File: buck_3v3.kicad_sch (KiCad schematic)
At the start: 20 parts, among them U6 TPS564257DRLR

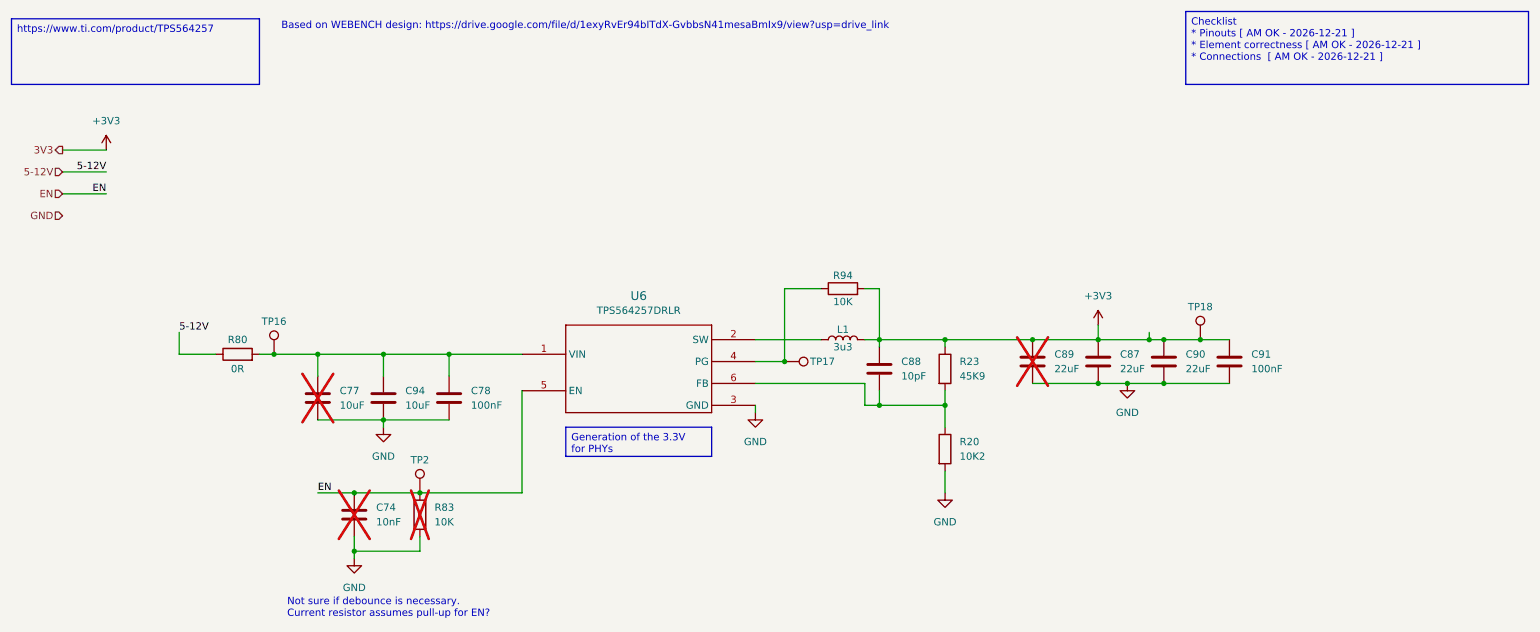
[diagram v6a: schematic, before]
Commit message: fixing issue related to symbol changes, and updating components
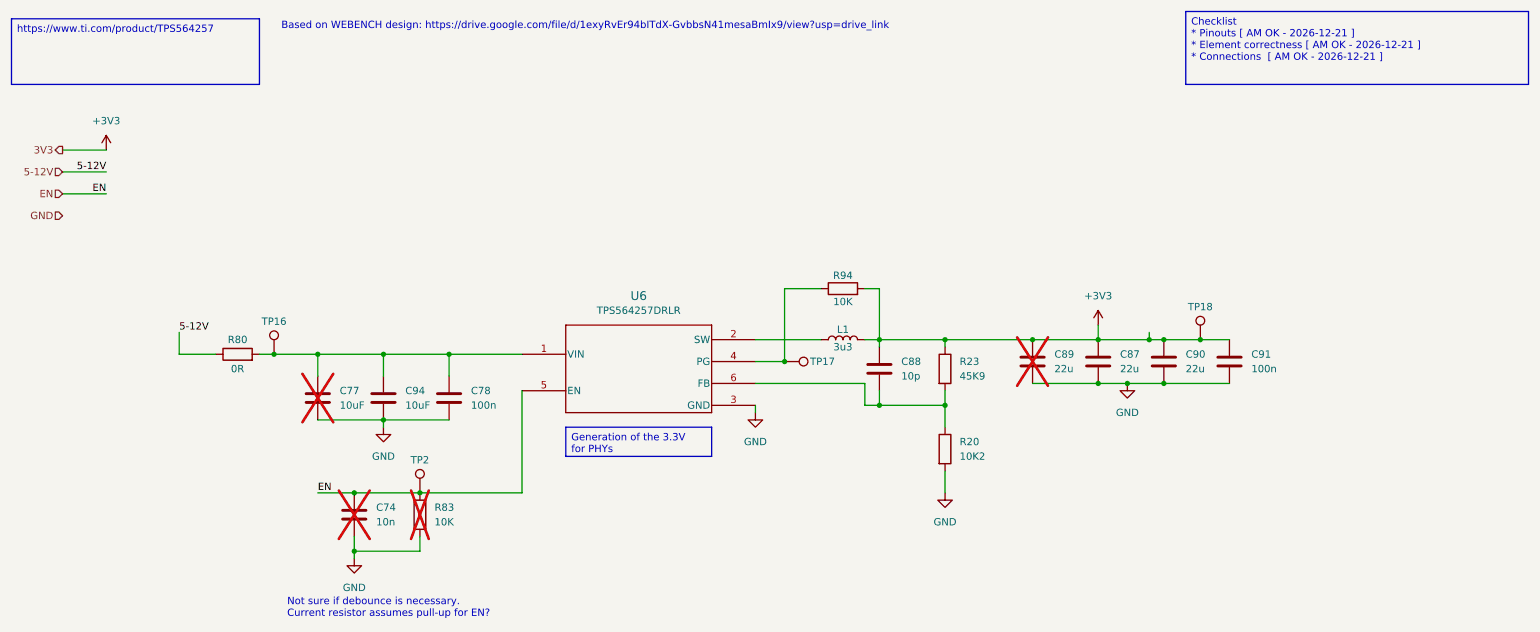
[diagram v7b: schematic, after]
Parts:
- C74: value 10nF -> 10n; footprint KL:C_0603 -> Capacitor_SMD:C_0201_0603Metric; symbol KL_C:C_10nF_25V_X7R_0603_20 -> KL_C:C_10n_50V_X7R_0603_10; Digikey 311-3111-1-ND -> 1276-CL10B103KB8WPNDCT-ND; LCSC C726559 -> C307346; Mouser 603-AC603KRX7R8BB103 -> 187-CL10B103KB8WPND; Tolerance 20 -> 10; Voltage 25 -> 50; now in the parts list
- C77, C94: footprint KL:C_0603 -> Capacitor_SMD:C_0201_0603Metric; symbol KL_C:C_10uF_25V_X5R_0603_20 -> KL_C:C_10u_25V_X5R_0603_20
- C78: value 100nF -> 100n; footprint KL:C_0603 -> Capacitor_SMD:C_0201_0603Metric; symbol KL_C:C_100nF_16V_X7R_0603_10 -> KL_C:C_100n_16V_X7R_0603_10
- C87, C89, C90: value 22uF -> 22u; symbol KL_C:C_22uF_10V_X5R_0603_20 -> KL_C:C_22u_10V_X5R_0603_20; Digikey 490-10476-1-ND -> 490-13243-1-ND; LCSC C84419 -> C361061; Mouser 81-GRM188R61A226ME5D -> 81-GRM187R61A226ME5D
- C88: value 10pF -> 10p; symbol KL_C:C_10pF_25V_C0G_0603_5 -> KL_C:C_10p_25V_C0G_0603_5
- C91: value 100nF -> 100n; footprint KL:C_0603 -> Capacitor_SMD:C_0201_0603Metric; symbol KL_C:C_100nF_10V_X7R_0603_10 -> KL_C:C_100n_10V_X7R_0603_10
- R20, R23, R83: footprint KL:R_0603 -> KL_Footprints:C_0603
- U6: footprint KL:SOT-563 -> KL_Footprints:SOT-563; symbol KL_IC_Power:TI_TPS564357DRLR -> KL_Voltage_Regulators:TPS564257DRLR; LCSC (none) -> C19272233; Mouser 595-TPS564257DRLR -> 595-TPS564257DRLR
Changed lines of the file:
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@@
 	)
 	(symbol
-		(lib_id "KL_C:C_10uF_25V_X5R_0603_20")
+		(lib_id "KL_C:C_10u_25V_X5R_0603_20")
 		(at 82.55 82.55 0)
 		(unit 1)
@@
 			)
 		)
-		(property "Footprint" "KL:C_0603"
+		(property "Footprint" "Capacitor_SMD:C_0201_0603Metric"
 			(at 83.5152 86.36 0)
 			(effects
@@
 	)
 	(symbol
-		(lib_id "KL_C:C_10pF_25V_C0G_0603_5")
+		(lib_id "KL_C:C_10p_25V_C0G_0603_5")
 		(at 168.91 77.47 0)
 		(unit 1)
@@
 			)
 		)
-		(property "Value" "10pF"
+		(property "Value" "10p"
 			(at 172.72 78.7399 0)
 			(effects
@@
 	)
 	(symbol
-		(lib_id "KL_C:C_10uF_25V_X5R_0603_20")
+		(lib_id "KL_C:C_10u_25V_X5R_0603_20")
 		(at 71.12 82.55 0)
 		(unit 1)
@@
 			)
 		)
-		(property "Footprint" "KL:C_0603"
+		(property "Footprint" "Capacitor_SMD:C_0201_0603Metric"
 			(at 72.0852 86.36 0)
 			(effects
@@
 	)
 	(symbol
-		(lib_id "KL_C:C_22uF_10V_X5R_0603_20")
+		(lib_id "KL_C:C_22u_10V_X5R_0603_20")
 		(at 195.58 76.2 0)
 		(unit 1)
@@
 			)
 		)
-		(property "Value" "22uF"
+		(property "Value" "22u"
 			(at 199.39 77.4699 0)
 			(effects
@@
 			)
 		)
-		(property "Mouser" "81-GRM188R61A226ME5D"
+		(property "Mouser" "81-GRM187R61A226ME5D"
 			(at 195.58 76.2 0)
 			(effects
@@
 			)
 		)
-		(property "Digikey" "490-10476-1-ND"
+		(property "Digikey" "490-13243-1-ND"
 			(at 195.58 76.2 0)
 			(effects
@@
 			)
 		)
-		(property "LCSC" "C84419"
+		(property "LCSC" "C361061"
 			(at 195.58 76.2 0)
 			(effects
@@
 	)
 	(symbol
-		(lib_id "KL_C:C_100nF_10V_X7R_0603_10")
+		(lib_id "KL_C:C_100n_10V_X7R_0603_10")
 		(at 229.87 76.2 0)
 		(unit 1)
@@
 			)
 		)
-		(property "Value" "100nF"
+		(property "Value" "100n"
 			(at 233.68 77.4699 0)
 			(effects
@@
 			)
 		)
-		(property "Footprint" "KL:C_0603"
+		(property "Footprint" "Capacitor_SMD:C_0201_0603Metric"
 			(at 230.8352 80.01 0)
 			(effects
@@
 	)
 	(symbol
-		(lib_id "KL_C:C_100nF_16V_X7R_0603_10")
+		(lib_id "KL_C:C_100n_16V_X7R_0603_10")
 		(at 93.98 82.55 0)
 		(unit 1)
@@
 			)
 		)
-		(property "Value" "100nF"
+		(property "Value" "100n"
 			(at 97.79 83.8199 0)
 			(effects
@@
 			)
 		)
-		(property "Footprint" "KL:C_0603"
+		(property "Footprint" "Capacitor_SMD:C_0201_0603Metric"
 			(at 94.9452 86.36 0)
 			(effects
@@
 			)
 		)
-		(property "Footprint" "KL:R_0603"
+		(property "Footprint" "KL_Footprints:C_0603"
 			(at 87.122 102.87 90)
 			(effects
@@
 	)
 	(symbol
-		(lib_name "R_10K_100mW_5_0603_1")
 		(lib_id "KL_R:R_10K_100mW_5_0603")
 		(at 162.56 63.5 90)
@@
 	)
 	(symbol
-		(lib_id "KL_C:C_10nF_25V_X7R_0603_20")
+		(lib_id "KL_C:C_10n_50V_X7R_0603_10")
 		(at 77.47 102.87 0)
 		(unit 1)
 		(exclude_from_sim no)
-		(in_bom no)
+		(in_bom yes)
 		(on_board yes)
 		(dnp yes)
@@
 			)
 		)
-		(property "Value" "10nF"
+		(property "Value" "10n"
 			(at 81.28 104.1399 0)
 			(effects
@@
 			)
 		)
-		(property "Footprint" "KL:C_0603"
+		(property "Footprint" "Capacitor_SMD:C_0201_0603Metric"
 			(at 78.4352 106.68 0)
 			(effects
@@
 			)
 		)
-		(property "Tolerance" "20"
+		(property "Tolerance" "10"
 			(at 77.47 102.87 0)
 			(effects
@@
 			)
 		)
-		(property "Voltage" "25"
+		(property "Voltage" "50"
 			(at 77.47 102.87 0)
 			(effects
@@
 			)
 		)
-		(property "Mouser" "603-AC603KRX7R8BB103"
+		(property "Mouser" "187-CL10B103KB8WPND"
 			(at 77.47 102.87 0)
 			(effects
@@
 			)
 		)
-		(property "Digikey" "311-3111-1-ND"
+		(property "Digikey" "1276-CL10B103KB8WPNDCT-ND"
 			(at 77.47 102.87 0)
 			(effects
@@
 			)
 		)
-		(property "LCSC" "C726559"
+		(property "LCSC" "C307346"
 			(at 77.47 102.87 0)
 			(effects
@@
 			)
 		)
-		(property "Footprint" "KL:R_0603"
+		(property "Footprint" "KL_Footprints:C_0603"
 			(at 178.562 77.47 90)
 			(effects
@@
 	)
 	(symbol
-		(lib_id "KL_IC_Power:TI_TPS564357DRLR")
-		(at 127 77.47 0)
+		(lib_id "KL_Voltage_Regulators:TPS564257DRLR")
+		(at 106.68 74.93 0)
 		(unit 1)
 		(exclude_from_sim no)
@@
 			)
 		)
-		(property "Footprint" "KL:SOT-563"
-			(at 127 72.39 0)
-			(effects
-				(font
-					(size 1.27 1.27)
-				)
-				(hide yes)
-			)
-		)
-		(property "Datasheet" ""
-			(at 127 72.39 0)
-			(effects
-				(font
-					(size 1.27 1.27)
+		(property "Footprint" "KL_Footprints:SOT-563"
+			(at 106.68 74.93 0)
+			(effects
+				(font
+					(size 1.27 1.27)
+					(italic yes)
+				)
+				(hide yes)
+			)
+		)
+		(property "Datasheet" "https://www.ti.com/lit/gpn/tps564257"
+			(at 106.68 74.93 0)
+			(effects
+				(font
+					(size 1.27 1.27)
+					(italic yes)
 				)
 				(hide yes)
@@
 		)
 		(property "Description" ""
-			(at 127 72.39 0)
-			(effects
-				(font
-					(size 1.27 1.27)
-				)
-				(hide yes)
-			)
-		)
-		(property "Mouser" "595-TPS564257DRLR"
-			(at 127 77.47 0)
+			(at 106.68 74.93 0)
+			(effects
+				(font
+					(size 1.27 1.27)
+				)
+				(hide yes)
+			)
+		)
+		(property "Mouser" " 595-TPS564257DRLR "
+			(at 106.68 74.93 0)
 			(effects
 				(font
@@
 		)
 		(property "Digikey" "296-TPS564257DRLRCT-ND"
-			(at 127 77.47 0)
+			(at 106.68 74.93 0)
 			(effects
 				(font
@@
 		)
 		(property "LSCS" "C19272233"
-			(at 127 77.47 0)
+			(at 106.68 74.93 0)
+			(effects
+				(font
+					(size 1.27 1.27)
+				)
+				(hide yes)
+			)
+		)
+		(property "LCSC" "C19272233"
+			(at 106.68 74.93 0)
 			(effects
 				(font
@@
 			)
 		)
-		(property "Footprint" "KL:R_0603"
+		(property "Footprint" "KL_Footprints:C_0603"
 			(at 178.562 91.44 90)
 			(effects
@@
 	)
 	(symbol
-		(lib_id "KL_C:C_22uF_10V_X5R_0603_20")
+		(lib_id "KL_C:C_22u_10V_X5R_0603_20")
 		(at 218.44 76.2 0)
 		(unit 1)
@@
 			)
 		)
-		(property "Value" "22uF"
+		(property "Value" "22u"
 			(at 222.25 77.4699 0)
 			(effects
@@
 			)
 		)
-		(property "Mouser" "81-GRM188R61A226ME5D"
+		(property "Mouser" "81-GRM187R61A226ME5D"
 			(at 218.44 76.2 0)
 			(effects
@@
 			)
 		)
-		(property "Digikey" "490-10476-1-ND"
+		(property "Digikey" "490-13243-1-ND"
 			(at 218.44 76.2 0)
 			(effects
@@
 			)
 		)
-		(property "LCSC" "C84419"
+		(property "LCSC" "C361061"
 			(at 218.44 76.2 0)
 			(effects
@@
 	)
 	(symbol
-		(lib_id "KL_C:C_22uF_10V_X5R_0603_20")
+		(lib_id "KL_C:C_22u_10V_X5R_0603_20")
 		(at 207.01 76.2 0)
 		(unit 1)
@@
 			)
 		)
-		(property "Value" "22uF"
+		(property "Value" "22u"
 			(at 210.82 77.4699 0)
 			(effects
@@
 			)
 		)
-		(property "Mouser" "81-GRM188R61A226ME5D"
+		(property "Mouser" "81-GRM187R61A226ME5D"
 			(at 207.01 76.2 0)
 			(effects
@@
 			)
 		)
-		(property "Digikey" "490-10476-1-ND"
+		(property "Digikey" "490-13243-1-ND"
 			(at 207.01 76.2 0)
 			(effects
@@
 			)
 		)
-		(property "LCSC" "C84419"
+		(property "LCSC" "C361061"
 			(at 207.01 76.2 0)
 			(effects

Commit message: updates all symbols to the project only paths. My bad - sorry
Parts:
- C77, C89, R83: now in the parts list
- U6: LSCS C19272233 -> (none)
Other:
- moved on the sheet: TP17
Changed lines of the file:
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@@
+	)
+	(junction
+		(at 153.67 63.5)
+		(diameter 0)
+		(color 0 0 0 0)
 	)
 	(junction
@@
 		(color 0 0 0 0)
 	)
-	(junction
-		(at 152.4 76.2)
-		(diameter 0)
-		(color 0 0 0 0)
-	)
 	(wire
 		(pts
@@
 	(wire
 		(pts
+			(xy 153.67 62.23) (xy 153.67 63.5)
+		)
+		(stroke
+			(width 0)
+			(type default)
+		)
+	)
+	(wire
+		(pts
 			(xy 168.91 73.66) (xy 168.91 72.39)
 		)
@@
 	(wire
 		(pts
+			(xy 153.67 63.5) (xy 152.4 63.5)
+		)
+		(stroke
+			(width 0)
+			(type default)
+		)
+	)
+	(wire
+		(pts
+			(xy 152.4 63.5) (xy 152.4 76.2)
+		)
+		(stroke
+			(width 0)
+			(type default)
+		)
+	)
+	(wire
+		(pts
 			(xy 166.37 72.39) (xy 168.91 72.39)
 		)
@@
 	(wire
 		(pts
-			(xy 152.4 63.5) (xy 152.4 76.2)
-		)
-		(stroke
-			(width 0)
-			(type default)
-		)
-	)
-	(wire
-		(pts
 			(xy 77.47 109.22) (xy 77.47 106.68)
 		)
@@
 	(wire
 		(pts
-			(xy 158.75 63.5) (xy 152.4 63.5)
+			(xy 158.75 63.5) (xy 153.67 63.5)
 		)
 		(stroke
@@
 		(unit 1)
 		(exclude_from_sim no)
-		(in_bom no)
+		(in_bom yes)
 		(on_board yes)
 		(dnp yes)
@@
 		(unit 1)
 		(exclude_from_sim no)
-		(in_bom no)
+		(in_bom yes)
 		(on_board yes)
 		(dnp yes)
@@
 	(symbol
 		(lib_id "KL_TP:TestPoint")
-		(at 152.4 76.2 270)
+		(at 153.67 62.23 0)
 		(unit 1)
 		(exclude_from_sim no)
@@
 		(fields_autoplaced yes)
 		(property "Reference" "TP17"
-			(at 159.004 76.2 90)
+			(at 153.67 56.515 0)
 			(do_not_autoplace yes)
 			(effects
@@
 		)
 		(property "Value" "~"
-			(at 157.48 76.2 0)
+			(at 153.67 57.15 0)
 			(effects
 				(font
@@
 		)
 		(property "Footprint" "Connector_PinHeader_2.54mm:PinHeader_1x01_P2.54mm_Vertical"
-			(at 152.4 81.28 0)
+			(at 158.75 62.23 0)
 			(effects
 				(font
@@
 		)
 		(property "Datasheet" "~"
-			(at 152.4 81.28 0)
+			(at 158.75 62.23 0)
 			(effects
 				(font
@@
 		)
 		(property "Description" "test point"
-			(at 152.4 76.2 0)
+			(at 153.67 62.23 0)
 			(effects
 				(font
@@
 		(unit 1)
 		(exclude_from_sim no)
-		(in_bom no)
+		(in_bom yes)
 		(on_board yes)
 		(dnp yes)
@@
 		(on_board yes)
 		(dnp no)
+		(fields_autoplaced yes)
 		(property "Reference" "R94"
-			(at 162.56 61.214 90)
+			(at 162.56 57.15 90)
 			(effects
 				(font
@@
 		)
 		(property "Value" "10K"
-			(at 162.56 65.786 90)
+			(at 162.56 59.69 90)
 			(effects
 				(font
@@
 			(effects
 				(font
-					(size 1.27 1.27)
+					(size 1.524 1.524)
 				)
 			)
@@
 		)
 		(property "Digikey" "296-TPS564257DRLRCT-ND"
-			(at 106.68 74.93 0)
-			(effects
-				(font
-					(size 1.27 1.27)
-				)
-				(hide yes)
-			)
-		)
-		(property "LSCS" "C19272233"
 			(at 106.68 74.93 0)
 			(effects
@@
 		(on_board yes)
 		(dnp no)
+		(fields_autoplaced yes)
 		(property "Reference" "R80"
-			(at 57.15 72.39 90)
+			(at 57.15 68.58 90)
 			(effects
 				(font
@@
 		)
 		(property "Value" "0R"
-			(at 57.15 77.47 90)
-			(effects
-				(font
+			(at 57.15 71.12 90)
+			(effects
+				(font
